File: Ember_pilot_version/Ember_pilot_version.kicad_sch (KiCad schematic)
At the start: 62 parts, among them J3 DROGUE, J4 BATT_CONN, J5 MAIN, J6 MAN2, J7 DROGUE2, J8 ARM, Q1 SISA96DN-T1, Q2 SISA96DN-T1, Q3 SISA96DN-T1, Q4 SISA96DN-T1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

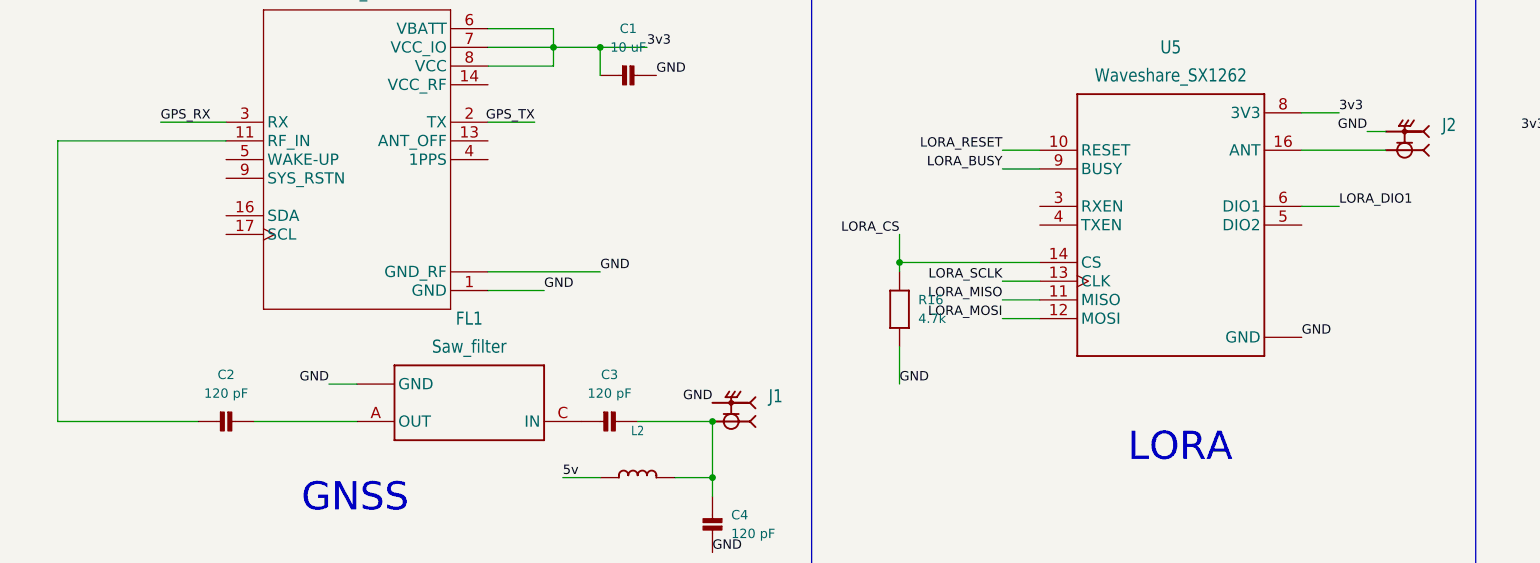
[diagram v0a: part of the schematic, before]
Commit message: RF traces done with some design changes
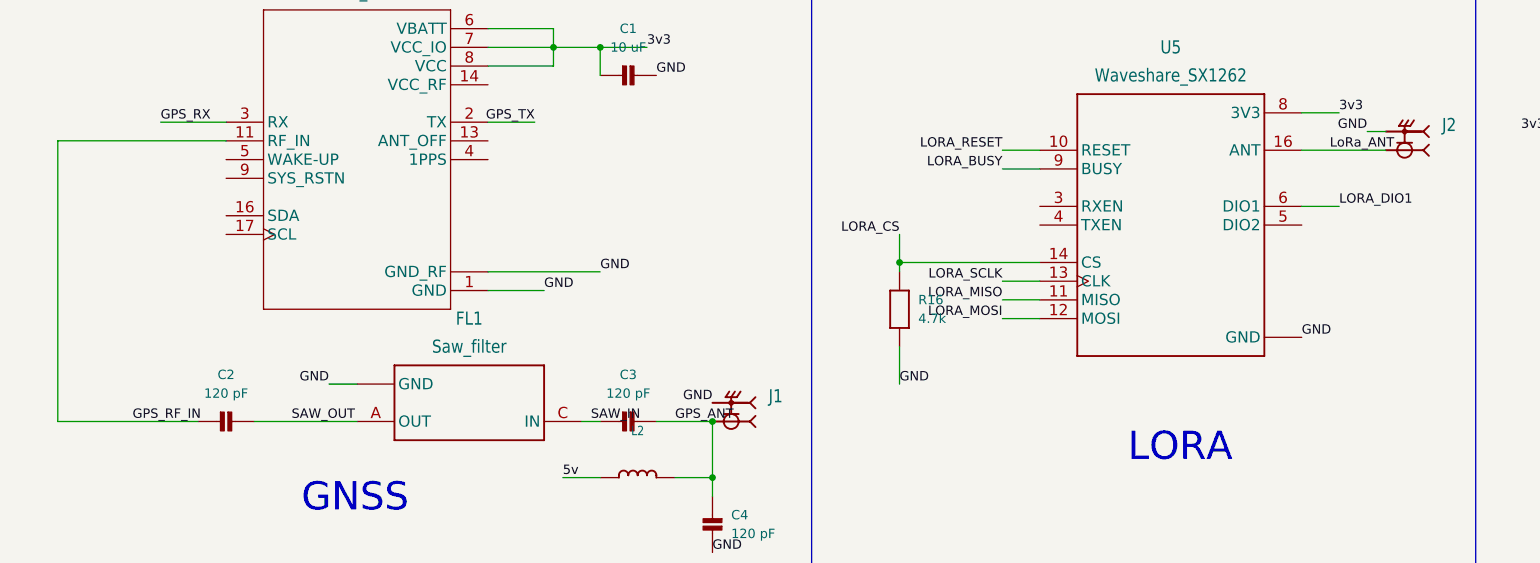
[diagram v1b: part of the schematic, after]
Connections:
- net LoRa_ANT: now reaches J2.1, U5.16 (ANT)
- net GPS_ANT: now reaches C3.1 (P$1), C4.2 (P$2), J1.1, L2.2
- net SAW_IN: now reaches C3.2 (P$2), FL1.C (IN)
- net SAW_OUT: now reaches C2.1 (P$1), FL1.A (OUT)
- net GPS_RF_IN: now reaches C2.2 (P$2), U6.11 (RF_IN)
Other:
- moved on the sheet: C3
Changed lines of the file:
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@@
 	)
 	(junction
+		(at 106.68 78.74)
+		(diameter 0)
+		(color 0 0 0 0)
+	)
+	(junction
 		(at 81.28 176.53)
 		(diameter 0)
@@
 	)
 	(junction
-		(at 106.68 78.74)
-		(diameter 0)
-		(color 0 0 0 0)
-	)
-	(junction
 		(at 36.83 172.72)
 		(diameter 0)
@@
 	(wire
 		(pts
-			(xy 96.52 78.74) (xy 106.68 78.74)
-		)
-		(stroke
-			(width 0)
-			(type default)
-		)
-	)
-	(wire
-		(pts
 			(xy 247.65 133.35) (xy 251.46 133.35)
 		)
@@
 	(wire
 		(pts
+			(xy 88.9 78.74) (xy 91.44 78.74)
+		)
+		(stroke
+			(width 0)
+			(type default)
+		)
+	)
+	(wire
+		(pts
 			(xy 17.78 78.74) (xy 36.83 78.74)
 		)
@@
 	(wire
 		(pts
+			(xy 99.06 78.74) (xy 106.68 78.74)
+		)
+		(stroke
+			(width 0)
+			(type default)
+		)
+	)
+	(wire
+		(pts
 			(xy 264.16 39.37) (xy 267.97 39.37)
 		)
@@
 		)
 	)
+	(label "SAW_IN"
+		(at 90.17 78.74 0)
+		(effects
+			(font
+				(size 1.27 1.27)
+			)
+			(justify left bottom)
+		)
+	)
 	(label "PYRO_MAIN"
 		(at 38.1 224.79 180)
@@
 		)
 	)
+	(label "LoRa_ANT"
+		(at 190.5 41.91 0)
+		(effects
+			(font
+				(size 1.27 1.27)
+			)
+			(justify left bottom)
+		)
+	)
 	(label "3v3"
 		(at 219.71 39.37 180)
@@
 		)
 	)
+	(label "SAW_OUT"
+		(at 49.53 78.74 0)
+		(effects
+			(font
+				(size 1.27 1.27)
+			)
+			(justify left bottom)
+		)
+	)
 	(label "GND"
 		(at 113.03 134.62 180)
@@
 		)
 	)
+	(label "GPS_ANT"
+		(at 101.6 78.74 0)
+		(effects
+			(font
+				(size 1.27 1.27)
+			)
+			(justify left bottom)
+		)
+	)
 	(label "XIN32"
 		(at 388.62 53.34 0)
@@
 		)
 	)
+	(label "GPS_RF_IN"
+		(at 27.94 78.74 0)
+		(effects
+			(font
+				(size 1.27 1.27)
+			)
+			(justify left bottom)
+		)
+	)
 	(label "GND"
 		(at 111.76 172.72 180)
@@
 	(symbol
 		(lib_id "microbuilder:CAP_CERAMIC0603")
-		(at 91.44 78.74 270)
+		(at 93.98 78.74 270)
 		(unit 1)
 		(exclude_from_sim no)
@@
 		(fields_autoplaced yes)
 		(property "Reference" "C3"
-			(at 92.71 72.39 90)
+			(at 95.25 72.39 90)
 			(effects
 				(font
@@
 		)
 		(property "Value" "120 pF"
-			(at 92.71 74.93 90)
+			(at 95.25 74.93 90)
 			(effects
 				(font
@@
 		)
 		(property "Footprint" "microbuilder:0603"
-			(at 91.44 78.74 0)
+			(at 93.98 78.74 0)
 			(effects
 				(font
@@
 		)
 		(property "Datasheet" ""
-			(at 91.44 78.74 0)
+			(at 93.98 78.74 0)
 			(effects
 				(font
@@
 		)
 		(property "Description" "Ceramic Capacitors\n\n0402 - 0402 Surface Mount Capacitors\n\n• 16pF 50V 5% [Digikey: 445-4899-2-ND]\n• 18pF 50V 5% [Digikey: 490-1281-2-ND]\n• 22pF 50V 5% [Digikey: 490-1283-2-ND]\n• 68pF 50V 5% [Digikey: 490-1289-2-ND]\n• 0.1uF 10V 10% [Digikey: 490-1318-2-ND]\n• 1.0uF 6.3V 10% [Digikey: 490-1320-2-ND]\n\n0603 - 0603 Surface Mount Capacitors\n\n• 16 pF 50V 5% [Digikey: 445-5051-2-ND]\n• 22 pF 50V [Digikey: PCC220ACVTR-ND]\n• 33 pF 50V 5% [Digikey: 490-1415-1-ND]\n• 56pF 50V 5% [Digikey: 490-1421-1-ND]\n• 220pF 50V 5% [Digikey: 445-1285-1-ND]\n• 680 pF 50V\n• 2200 pF 50V 5% C0G [Digikey: 445-1297-1-ND]\n• 5600 pF 100V 5% X7R [Digikey: 478-3711-1-ND]\n• 0.1 µF 25V 10% [Digikey: PCC2277TR-ND]\n• 0.22 µF 16V 10% X7R [Digikey: 445-1318-1-ND]\n• 1.0 µF 25V 10% [Digikey: 445-5146-2-ND]\n\n0603 - RF Specific\n\n• 3pF 250V +/-0.1pF RF [Digikey: 712-1347-1-ND]\n• 18 pF 250V 5%  [Digikey: 478-3505-1-ND or 712-1322-1-ND]\n• 56 pF 250V 5% C0G RF [Digikey: 490-4867-1-ND]\n• 68 pF 250V RF [Digikey: 490-4868-1-ND]\n\n0805 - 0805 Surface Mount Capacitors\n\n• 220 pF 250V 2% RF Ceramic Capacitor [Digikey: 712-1398-1-ND]\n• 1000 pF 50V 2% NP0 Ceramic Capacitor [Digikey: 478-3760-1-ND]\n• 0.1 µF 25V 10% Ceramic Capacitor [Digikey: PCC1828TR-ND]\n• 1.0 µF 16V 10% Ceramic Capacitor[Digikey: 490-1691-2-ND]\n• 10.0 µF 10V 10% Ceramic Capacitor[Digikey: 709-1228-1-ND]\n• 10.0 uF 16V 10% Ceramic Capacitor [Digikey: 478-5165-2-ND]\n• 47 uF 6.3V 20% Ceramic Capacitor [Digikey: 587-1779-1-ND or 399-5506-1-ND]\n\n1206 - 1206 Surface Mount Capacitors\n\n• 47uF 10V 20% Ceramic Capacitor [Digikey: 490-5528-1-ND or 399-5508-1-ND or 445-6010-1-ND]\n• 100uF 6.3V -20%, +80% Y5V Ceramic Capacitor (Digikey: 490-4512-1-ND, Mouser: 81-GRM31CF50J107ZE1L)"
-			(at 91.44 78.74 0)
+			(at 93.98 78.74 0)
 			(effects
 				(font
